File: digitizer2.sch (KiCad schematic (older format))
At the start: 10 parts, among them U1 XC7A35T, U2 FT2232H, U3 MT41J128M16, U4 ADS5403, U5 LTC3569, U6 TPS79618DCQ, U7 TPS79633DCQ, U8 93LC46BT-I/OT

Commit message: Work on power supply
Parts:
- added C1, C11, C12, C13, C14, C15, C16, C17, C22, C8: 100nF, Capacitors_SMD:C_0603, symbol C
- added C10, C21, C23, C24, C25, C26, C27, C28, C29, C3, C5, C7, C9: 4.7uF, Capacitors_SMD:C_0603, symbol C
- added C18, C19, C20: 20pF, Capacitors_SMD:C_0603, symbol C_Small
- added C2: 22uF, Capacitors_SMD:C_0603, symbol C
- added C4, C6: 18pF, Capacitors_SMD:C_0603, symbol C
- added L1, L2: ferrite, Resistors_SMD:R_0603, symbol INDUCTOR
- added L3, L5: 2.2uH, digitizer2_modules:IHLP-1212BZ-11, symbol INDUCTOR_SMALL
- added L4: 3.3uH, digitizer2_modules:IHLP-1212BZ-11, symbol INDUCTOR_SMALL
- added L6: 2.2uH, digitizer2_modules:IHLP-1212BZ-11, symbol INDUCTOR
- added P1: USB_OTG, Connect:USB_Micro-B, symbol USB_OTG
- added R10: 175k, Resistors_SMD:R_0603, symbol R_Small
- added R11, R15: 200k, Resistors_SMD:R_0603, symbol R_Small
- added R12: 125k, Resistors_SMD:R_0603, symbol R_Small
- added R13: 100k, Resistors_SMD:R_0603, symbol R_Small
- added R14: 50k, Resistors_SMD:R_0603, symbol R_Small
- added R3, R4, R7, R8: 10k, Resistors_SMD:R_0603, symbol R
- added R5: 2.2k, Resistors_SMD:R_0603, symbol R
- added R6: 200k, Resistors_SMD:R_0603, symbol R
- added R9: 12k, Resistors_SMD:R_0603, symbol R
- added U9: LM3671MF-3.3, symbol LM3671MF-3.3
- added Y1: 12MHz, symbol Crystal
- R1, R2: footprint (none) -> Resistors_SMD:R_0603
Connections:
- net GND: now also U1.F8 (VCCBATT_0), U5.10 (SGND), U5.14 (PGND3), U5.19 (PGND1), U5.20 (PGND2), U5.21 (PAD), U8.2 (GND), C1.2, C10.2, C11.2, C12.2, C13.2, C14.2, C15.2, C16.2, C17.2, C2.2, C21.2, C22.2, C23.2, C24.2, C25.2, C26.2, C27.2, C28.2, C29.2, C3.2, C4.2, C5.2, C6.2, C7.2, C8.2, C9.2, R11.2, R13.2, R15.2, R6.2, R9.2, U9.2 (GND)
- net USB_CON_D_N: now also P1.2 (D-)
- net USB_CON_D_P: now also P1.3 (D+)
- net VDD_DRAM_1V5: now also C18.1, C23.1, C27.1, L3.2, R10.1
- net VDD_FPGA_1V0: now also C20.1, C25.1, C29.1, L5.2, R14.1
- net VDD_FPGA_1V8: now also C19.1, C24.1, C28.1, L4.2, R12.1; no longer U1.F8 (VCCBATT_0)
- net VDD_FPGA_3V3: now also U8.6 (VCC), C1.1, C15.1, C16.1, C17.1, C21.1, C22.1, C26.1, L1.2, L2.2, L6.1, R3.2, R4.1, R7.1, R8.1, U9.4 (FB)
- net VDD_FTDI_1V8: now also C11.1, C13.1, C14.1, C9.1
- net USB_RESET: now reaches U2.14 (~RESET)
- net USB_RESET: now also R3.1
- net at U2.2 (OSCI): now also C4.1, Y1.1
- net at U2.3 (OSCO): now also C6.1, Y1.2
- net at U2.4 (VPHY): now also C12.1, C5.1, L2.1
- net at U2.6 (REF): now also R9.1
- net at U2.61 (EEDATA): now also U8.3 (DI), R5.1, R8.2
- net at U2.62 (EECLK): now also U8.4 (CLK), R7.2
- net at U2.63 (EECS): now also U8.5 (CS), R4.2
- net at U2.9 (VPLL): now also C3.1, C8.1, L1.1
- net at U5.1 (SW2): now also L4.1
- net 5V0: now reaches U5.11 (EN3)
- net 5V0: now also U5.12 (EN2), U5.13 (EN1), U5.16 (PVIN3), U5.17 (PVIN1), U5.2 (PVIN2), U5.4 (MODE), U5.9 (SVIN), C10.1, C2.1, C7.1, U9.1 (VIN), U9.3 (EN)
- net at U5.15 (SW3): now also L5.1
- net at U5.18 (SW1): now also L3.1
- net at U5.5 (RT): now also R6.1
- net at U5.6 (FB2): now also C19.2, R12.2, R13.1
- net at U5.7 (FB1): now also C18.2, R10.2, R11.1
- net at U5.8 (FB3): now also C20.2, R14.2, R15.1
- net at U8.1 (DO): now also R5.2
- new net: L6.2, U9.5 (SW)
- new net USB_5V0: P1.1 (VCC)
- new net USB_GND: P1.5 (GND)
- new net USB_SHD: P1.6 (shield)
- no-connect marks 27 -> 105
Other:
- note added: "=1.76 MHz"
- note added: "FB=0.8V"
- moved on the sheet: U2, U3, U4, U5, U6, U7, U8

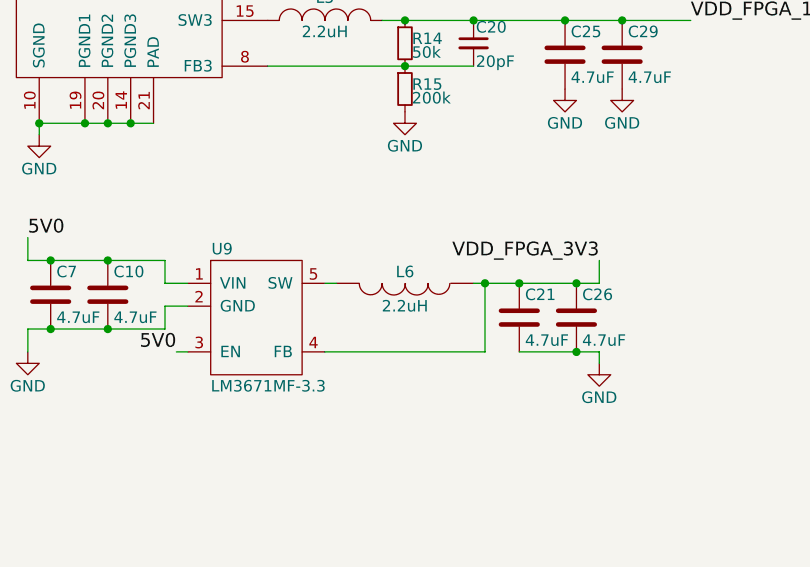
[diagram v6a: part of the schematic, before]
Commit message: Start routing power supply
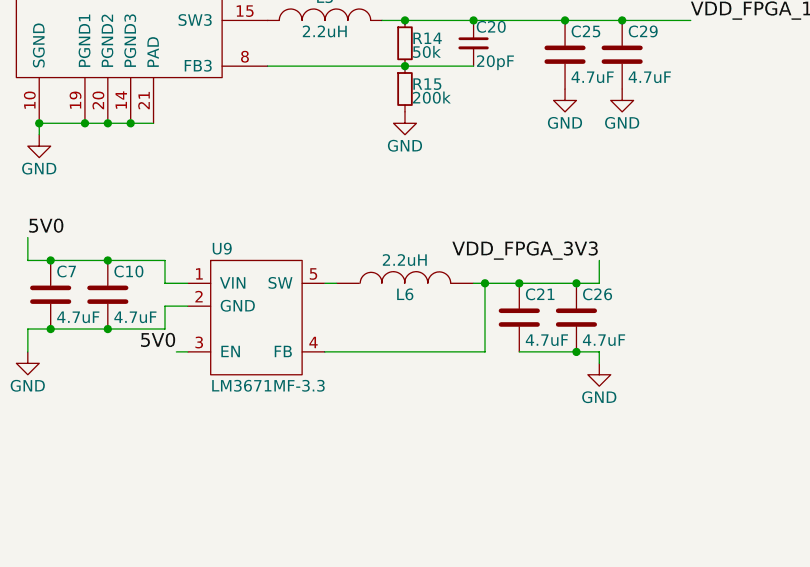
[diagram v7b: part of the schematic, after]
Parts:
- U9: footprint (none) -> TO_SOT_Packages_SMD:SOT-23-6
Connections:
- net VDD_FPGA_3V3: now also L6.2; no longer L6.1
- net at U9.5 (SW): now also L6.1; no longer L6.2
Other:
- moved on the sheet: L6
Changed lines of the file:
@@
 VDD_FPGA_3V3
 $Comp
-L GND #PWR010
+L GND #PWR08
 U 1 1 56EBFCD0
 P 850 20400
-F 0 "#PWR010" H 850 20150 50  0001 C CNN
+F 0 "#PWR08" H 850 20150 50  0001 C CNN
 F 1 "GND" H 850 20250 50  0000 C CNN
 F 2 "" H 850 20400 50  0000 C CNN
@@
 $EndComp
 $Comp
-L GND #PWR011
+L GND #PWR09
 U 1 1 56ECA829
 P 2150 19350
-F 0 "#PWR011" H 2150 19100 50  0001 C CNN
+F 0 "#PWR09" H 2150 19100 50  0001 C CNN
 F 1 "GND" H 2150 19200 50  0000 C CNN
 F 2 "" H 2150 19350 50  0000 C CNN
@@
 $EndComp
 $Comp
-L GND #PWR012
+L GND #PWR010
 U 1 1 56ECE125
 P 2400 17950
-F 0 "#PWR012" H 2400 17700 50  0001 C CNN
+F 0 "#PWR010" H 2400 17700 50  0001 C CNN
 F 1 "GND" H 2400 17800 50  0000 C CNN
 F 2 "" H 2400 17950 50  0000 C CNN
@@
 $EndComp
 $Comp
-L GND #PWR013
+L GND #PWR011
 U 1 1 56ED0940
 P 1600 17850
-F 0 "#PWR013" H 1600 17600 50  0001 C CNN
+F 0 "#PWR011" H 1600 17600 50  0001 C CNN
 F 1 "GND" H 1600 17700 50  0000 C CNN
 F 2 "" H 1600 17850 50  0000 C CNN
@@
 $EndComp
 $Comp
-L GND #PWR014
+L GND #PWR012
 U 1 1 56ED5F98
 P 2450 21150
-F 0 "#PWR014" H 2450 20900 50  0001 C CNN
+F 0 "#PWR012" H 2450 20900 50  0001 C CNN
 F 1 "GND" H 2450 21000 50  0000 C CNN
 F 2 "" H 2450 21150 50  0000 C CNN
@@
 $EndComp
 $Comp
-L GND #PWR015
+L GND #PWR013
 U 1 1 56ED6025
 P 2200 21150
-F 0 "#PWR015" H 2200 20900 50  0001 C CNN
+F 0 "#PWR013" H 2200 20900 50  0001 C CNN
 F 1 "GND" H 2200 21000 50  0000 C CNN
 F 2 "" H 2200 21150 50  0000 C CNN
@@
 $EndComp
 $Comp
-L GND #PWR016
+L GND #PWR014
 U 1 1 56ED607E
 P 1950 21150
-F 0 "#PWR016" H 1950 20900 50  0001 C CNN
+F 0 "#PWR014" H 1950 20900 50  0001 C CNN
 F 1 "GND" H 1950 21000 50  0000 C CNN
 F 2 "" H 1950 21150 50  0000 C CNN
@@
 VDD_FTDI_1V8
 $Comp
-L GND #PWR017
+L GND #PWR015
 U 1 1 56EDEA49
 P 3500 16250
-F 0 "#PWR017" H 3500 16000 50  0001 C CNN
+F 0 "#PWR015" H 3500 16000 50  0001 C CNN
 F 1 "GND" H 3500 16100 50  0000 C CNN
 F 2 "" H 3500 16250 50  0000 C CNN
@@
 $EndComp
 $Comp
-L GND #PWR018
+L GND #PWR016
 U 1 1 56EDEF5B
 P 2600 16250
-F 0 "#PWR018" H 2600 16000 50  0001 C CNN
+F 0 "#PWR016" H 2600 16000 50  0001 C CNN
 F 1 "GND" H 2600 16100 50  0000 C CNN
 F 2 "" H 2600 16250 50  0000 C CNN
@@
 $EndComp
 $Comp
-L GND #PWR019
+L GND #PWR017
 U 1 1 56EE4107
 P 2600 17200
-F 0 "#PWR019" H 2600 16950 50  0001 C CNN
+F 0 "#PWR017" H 2600 16950 50  0001 C CNN
 F 1 "GND" H 2600 17050 50  0000 C CNN
 F 2 "" H 2600 17200 50  0000 C CNN
@@
 $EndComp
 $Comp
-L GND #PWR020
+L GND #PWR018
 U 1 1 56EE4D9D
 P 2300 17200
-F 0 "#PWR020" H 2300 16950 50  0001 C CNN
+F 0 "#PWR018" H 2300 16950 50  0001 C CNN
 F 1 "GND" H 2300 17050 50  0000 C CNN
 F 2 "" H 2300 17200 50  0000 C CNN
@@
 $EndComp
 $Comp
-L GND #PWR021
+L GND #PWR019
 U 1 1 56EE4E17
 P 2000 17200
-F 0 "#PWR021" H 2000 16950 50  0001 C CNN
+F 0 "#PWR019" H 2000 16950 50  0001 C CNN
 F 1 "GND" H 2000 17050 50  0000 C CNN
 F 2 "" H 2000 17200 50  0000 C CNN
@@
 $EndComp
 $Comp
-L GND #PWR022
+L GND #PWR020
 U 1 1 56EE4E91
 P 1700 17200
-F 0 "#PWR022" H 1700 16950 50  0001 C CNN
+F 0 "#PWR020" H 1700 16950 50  0001 C CNN
 F 1 "GND" H 1700 17050 50  0000 C CNN
 F 2 "" H 1700 17200 50  0000 C CNN
@@
 F 0 "U9" H 3050 12650 50  0000 C CNN
 F 1 "LM3671MF-3.3" H 3000 12050 50  0000 L CNN
-F 2 "" H 3100 12300 50  0000 C CNN
+F 2 "TO_SOT_Packages_SMD:SOT-23-6" H 3100 12300 50  0001 C CNN
 F 3 "" H 3200 12400 50  0000 C CNN
 	1    3200 12300
@@
 F 3 "" H 3850 12100 50  0000 C CNN
 	1    3850 12100
-	0    1    1    0
+	0    -1   -1   0
 $EndComp
 Wire Wire Line
@@
 5V0
 $Comp
-L GND #PWR023
+L GND #PWR021
 U 1 1 56F20B7E
 P 2200 12400
-F 0 "#PWR023" H 2200 12150 50  0001 C CNN
+F 0 "#PWR021" H 2200 12150 50  0001 C CNN
 F 1 "GND" H 2200 12250 50  0000 C CNN
 F 2 "" H 2200 12400 50  0000 C CNN
@@
 $EndComp
 $Comp
-L GND #PWR024
+L GND #PWR022
 U 1 1 56F21343
 P 4700 12450
-F 0 "#PWR024" H 4700 12200 50  0001 C CNN
+F 0 "#PWR022" H 4700 12200 50  0001 C CNN
 F 1 "GND" H 4700 12300 50  0000 C CNN
 F 2 "" H 4700 12450 50  0000 C CNN
@@
 $EndComp
 $Comp
-L GND #PWR025
+L GND #PWR023
 U 1 1 56F55FEC
 P 1650 10250
-F 0 "#PWR025" H 1650 10000 50  0001 C CNN
+F 0 "#PWR023" H 1650 10000 50  0001 C CNN
 F 1 "GND" H 1650 10100 50  0000 C CNN
 F 2 "" H 1650 10250 50  0000 C CNN
@@
 $EndComp
 $Comp
-L GND #PWR026
+L GND #PWR024
 U 1 1 56F5FCCA
 P 3850 10650
-F 0 "#PWR026" H 3850 10400 50  0001 C CNN
+F 0 "#PWR024" H 3850 10400 50  0001 C CNN
 F 1 "GND" H 3850 10500 50  0000 C CNN
 F 2 "" H 3850 10650 50  0000 C CNN
@@
 Connection ~ 4550 10250
 $Comp
-L GND #PWR027
+L GND #PWR025
 U 1 1 56F62F16
 P 4550 10550
-F 0 "#PWR027" H 4550 10300 50  0001 C CNN
+F 0 "#PWR025" H 4550 10300 50  0001 C CNN
 F 1 "GND" H 4550 10400 50  0000 C CNN
 F 2 "" H 4550 10550 50  0000 C CNN
@@
 $EndComp
 $Comp
-L GND #PWR028
+L GND #PWR026
 U 1 1 56F62FC0
 P 4800 10550
-F 0 "#PWR028" H 4800 10300 50  0001 C CNN
+F 0 "#PWR026" H 4800 10300 50  0001 C CNN
 F 1 "GND" H 4800 10400 50  0000 C CNN
 F 2 "" H 4800 10550 50  0000 C CNN
@@
 $EndComp
 $Comp
-L GND #PWR029
+L GND #PWR027
 U 1 1 56F638A5
 P 3850 11350
-F 0 "#PWR029" H 3850 11100 50  0001 C CNN
+F 0 "#PWR027" H 3850 11100 50  0001 C CNN
 F 1 "GND" H 3850 11200 50  0000 C CNN
 F 2 "" H 3850 11350 50  0000 C CNN
@@
 Connection ~ 3850 11150
 $Comp
-L GND #PWR030
+L GND #PWR028
 U 1 1 56F652F1
 P 3850 9950
-F 0 "#PWR030" H 3850 9700 50  0001 C CNN
+F 0 "#PWR028" H 3850 9700 50  0001 C CNN
 F 1 "GND" H 3850 9800 50  0000 C CNN
 F 2 "" H 3850 9950 50  0000 C CNN
@@
 $EndComp
 $Comp
-L GND #PWR031
+L GND #PWR029
 U 1 1 56F6580C
 P 4550 11250
-F 0 "#PWR031" H 4550 11000 50  0001 C CNN
+F 0 "#PWR029" H 4550 11000 50  0001 C CNN
 F 1 "GND" H 4550 11100 50  0000 C CNN
 F 2 "" H 4550 11250 50  0000 C CNN
@@
 $EndComp
 $Comp
-L GND #PWR032
+L GND #PWR030
 U 1 1 56F658D4
 P 4800 11250
-F 0 "#PWR032" H 4800 11000 50  0001 C CNN
+F 0 "#PWR030" H 4800 11000 50  0001 C CNN
 F 1 "GND" H 4800 11100 50  0000 C CNN
 F 2 "" H 4800 11250 50  0000 C CNN
@@
 	2250 11400 2250 11450
 $Comp
-L GND #PWR033
+L GND #PWR031
 U 1 1 56F6E6E1
 P 2250 11450
-F 0 "#PWR033" H 2250 11200 50  0001 C CNN
+F 0 "#PWR031" H 2250 11200 50  0001 C CNN
 F 1 "GND" H 2250 11300 50  0000 C CNN
 F 2 "" H 2250 11450 50  0000 C CNN
@@
 Connection ~ 1650 9250
 $Comp
-L GND #PWR034
+L GND #PWR032
 U 1 1 56F70B41
 P 4550 9850
-F 0 "#PWR034" H 4550 9600 50  0001 C CNN
+F 0 "#PWR032" H 4550 9600 50  0001 C CNN
 F 1 "GND" H 4550 9700 50  0000 C CNN
 F 2 "" H 4550 9850 50  0000 C CNN
@@
 $EndComp
 $Comp
-L GND #PWR035
+L GND #PWR033
 U 1 1 56F70C15
 P 4800 9850
-F 0 "#PWR035" H 4800 9600 50  0001 C CNN
+F 0 "#PWR033" H 4800 9600 50  0001 C CNN
 F 1 "GND" H 4800 9700 50  0000 C CNN
 F 2 "" H 4800 9850 50  0000 C CNN
@@
 $EndComp
 $Comp
-L GND #PWR036
+L GND #PWR034
 U 1 1 56F70CE9
 P 1650 9550
-F 0 "#PWR036" H 1650 9300 50  0001 C CNN
+F 0 "#PWR034" H 1650 9300 50  0001 C CNN
 F 1 "GND" H 1650 9400 50  0000 C CNN
 F 2 "" H 1650 9550 50  0000 C CNN
@@
 	5050 10250 5050 10250
 $Comp
-L GND #PWR?
+L GND #PWR035
 U 1 1 56FC8EEE
 P 3750 26350
-F 0 "#PWR?" H 3750 26100 50  0001 C CNN
+F 0 "#PWR035" H 3750 26100 50  0001 C CNN
 F 1 "GND" H 3750 26200 50  0000 C CNN
 F 2 "" H 3750 26350 50  0000 C CNN
@@
 $EndComp
 $Comp
-L GND #PWR?
+L GND #PWR036
 U 1 1 56FC95D1
 P 3750 26650
-F 0 "#PWR?" H 3750 26400 50  0001 C CNN
+F 0 "#PWR036" H 3750 26400 50  0001 C CNN
 F 1 "GND" H 3750 26500 50  0000 C CNN
 F 2 "" H 3750 26650 50  0000 C CNN
@@
 $EndComp
 $Comp
-L GND #PWR?
+L GND #PWR037
 U 1 1 56FC96A2
 P 3750 26950
-F 0 "#PWR?" H 3750 26700 50  0001 C CNN
+F 0 "#PWR037" H 3750 26700 50  0001 C CNN
 F 1 "GND" H 3750 26800 50  0000 C CNN
 F 2 "" H 3750 26950 50  0000 C CNN

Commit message: Power supply and bypass capacitors
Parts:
- added C100, C101, C102, C103, C110, C111, C112, C113, C114, C115, C36, C37, C74, C75, C76, C77, C78, C79, C86, C87, C88, C89, C90, C91, C98, C99, C? (x2): 10nF, Capacitors_SMD:C_0402, symbol C_Small
- added C104, C105, C106, C107, C108, C109, C116, C117, C118, C119, C120, C121, C80, C81, C82, C83, C84, C85, C92, C93, C94, C95, C96, C97: 100nF, Capacitors_SMD:C_0402, symbol C_Small
- added C30, C31, C32, C? (x4): 4.7uF, Capacitors_SMD:C_0402, symbol C
- added C33, C34: 100nF, Capacitors_SMD:C_0402, symbol C
- added C35: 1uF, Capacitors_SMD:C_0402, symbol C_Small
- added C38, C39, C40, C44, C45, C46, C51, C53, C54, C55, C56, C60, C61, C62, C63, C67, C68, C69, C70: 470nF, Capacitors_SMD:C_0402, symbol C_Small
- added C41, C42, C47, C48, C57, C58, C64, C65, C71, C72: 4.7uF, Capacitors_SMD:C_0402, symbol C_Small
- added C43, C49, C50, C52, C59, C66, C73: 47uF, Capacitors_SMD:C_0402, symbol C_Small
- added L? (x2): ferrite, Resistors_SMD:R_0603, symbol INDUCTOR
- added R16: 100, Resistors_SMD:R_0402, symbol R
- added R17, R18: 1k, Resistors_SMD:R_0402, symbol R_Small
- added R19: 100, Resistors_SMD:R_0402, symbol R_Small
- added R20: 240, Resistors_SMD:R_0402, symbol R_Small
- C1, C10, C11, C12, C13, C14, C15, C16, C17, C21, C22, C23, C24, C25, C26, C27, C28, C29, C3, C5, C7, C8, C9: footprint Capacitors_SMD:C_0603 -> Capacitors_SMD:C_0402
- C2: value 22uF -> 4.7uF; footprint Capacitors_SMD:C_0603 -> Capacitors_SMD:C_0402
- R1, R2: footprint Resistors_SMD:R_0603 -> Resistors_SMD:R_0402
- Y1: footprint (none) -> Crystals:Crystal_SMD_5032_2Pads
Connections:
- net 5V0: now also C30.1, C31.1, C32.1
- net ADC_CLKIN_N: now also C34.1
- net ADC_CLKIN_P: now also C33.1
- net ADC_SAMPLE_CLK_N: now also C34.2, R16.1
- net ADC_SAMPLE_CLK_P: now also C33.2, R16.2
- net DRAM_CK_N: now also R19.2
- net DRAM_CK_P: now also R19.1
- net DRAM_ZQ: now also R20.1
- net GND: now also U6.3 (GND), U6.6 (PAD), U7.3 (GND), U7.6 (PAD), C100.2, C101.2, C102.2, C103.2, C104.2, C105.2, C106.2, C107.2, C108.2, C109.2, C110.2, C111.2, C112.2, C113.2, C114.2, C115.2, C116.2, C117.2, C118.2, C119.2, C120.2, C121.2, C30.2, C31.2, C32.2, C35.2, C37.2, C38.2, C39.2, C40.2, C41.2, C42.2, C43.2, C44.2, C45.2, C46.2, C47.2, C48.2, C49.2, C50.2, C51.2, C52.2, C53.2, C54.2, C55.2, C56.2, C57.2, C58.2, C59.2, C60.2, C61.2, C62.2, C63.2, C64.2, C65.2, C66.2, C67.2, C68.2, C69.2, C70.2, C71.2, C72.2, C73.2, C74.2, C75.2, C76.2, C77.2, C78.2, C79.2, C80.2, C81.2, C82.2, C83.2, C84.2, C85.2, C86.2, C87.2, C88.2, C89.2, C90.2, C91.2, C92.2, C93.2, C94.2, C95.2, C96.2, C97.2, C98.2, C99.2, C?.2, C?.2, C?.2, C?.2, C?.2, C?.2, R18.2, R20.2
- net VDD_ADC_1V8: now also U1.M3 (VCCO_34), U1.R4 (VCCO_34), U1.T1 (VCCO_34), U4.B10 (IOVDD), U6.4 (OUT), C100.1, C101.1, C102.1, C103.1, C104.1, C105.1, C106.1, C107.1, C108.1, C109.1, C67.1, C68.1, C69.1, C70.1, C71.1, C72.1, C73.1, C86.1, C87.1, C88.1, C89.1, C90.1, C91.1, C92.1, C93.1, C94.1, C95.1, C96.1, C97.1, C98.1, C99.1, C?.1
- net VDD_ADC_3V3: now also U7.4 (OUT), C74.1, C75.1, C76.1, C77.1, C78.1, C79.1, C80.1, C81.1, C82.1, C83.1, C84.1, C85.1, C?.1
- net VDD_DRAM_1V5: now also C110.1, C111.1, C112.1, C113.1, C114.1, C115.1, C116.1, C117.1, C118.1, C119.1, C120.1, C121.1, C36.1, C60.1, C61.1, C62.1, C63.1, C64.1, C65.1, C66.1, R17.1
- net VDD_FPGA_1V0: now also C44.1, C45.1, C46.1, C47.1, C48.1, C49.1, C50.1, C51.1, C52.1
- net VDD_FPGA_1V8: now also C38.1, C39.1, C40.1, C41.1, C42.1, C43.1
- net VDD_FPGA_3V3: now also C53.1, C54.1, C55.1, C56.1, C57.1, C58.1, C59.1
- net GCLK_N: now reaches U1.C4 (IO_L12N_T1_MRCC_35)
- net GCLK_P: now reaches U1.D4 (IO_L12P_T1_MRCC_35)
- net DRAM_Vref: now reaches U3.H1 (VrefDQ)
- net DRAM_Vref: now also U3.M8 (VrefCA), C35.1, C36.2, C37.1, R17.2, R18.1
- net at U6.1 (EN): now also U6.2 (IN), C?.1, L?.1
- net at U6.5 (NR): now also C?.1
- net at U7.1 (EN): now also U7.2 (IN), C?.1, L?.1
- net at U7.5 (NR): now also C?.1
- new net A5V0: L?.2, L?.2
- no-connect marks 105 -> 103
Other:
- moved on the sheet: C1, C11, C12, C13, C14, C15, C16, C17, C22, C3, C4, C5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
